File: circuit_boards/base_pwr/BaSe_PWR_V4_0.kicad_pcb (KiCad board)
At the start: 4 copper layers, 114.2 x 101.5 mm, 103 parts, among them J1 12VDC In, J10 Conn_01x04_Socket, J11 MOTOR, J12 USB3_A, J3 USB_B_Micro, J4 Conn_01x07_Pin, J5 Conn_02x06_Odd_Even, J6 USB3_B_Micro, J7 Conn_02x06_Odd_Even, J8 USB_C_Receptacle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

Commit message: almost finished layout
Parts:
- moved R4 3.05 mm to (82.8, 79.7), turned to 90 degrees
- moved D2 3.03 mm to (35.9, 85.0)
- moved R5 0.25 mm to (81.3, 83.0)
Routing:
- net /Taster_1: track 0.00 -> 34.6 mm, vias 0 -> 1
- net GND: track 18.7 -> 44.9 mm, vias 34 -> 56
- net /Taster_0: track 0.00 -> 24.2 mm, vias 0 -> 1
- net +3V3_STBY: track 12.2 -> 32.0 mm, vias 0 -> 9
- net /hmi_pwm0: track 0.00 -> 12.3 mm
- net /hmi_pwm1: track 0.00 -> 10.9 mm
- net /sw_sbu_on: track 37.1 -> 42.7 mm
- net /Dis_PWM: track 0.00 -> 4.32 mm
- net /LED_HMI: track 0.00 -> 4.26 mm
- net /sw_sbu_off: track 38.1 -> 41.4 mm
- net +5V: track 134.2 -> 136.5 mm
- net /vbus_sense: track 46.4 -> 45.7 mm
- net /~{LM2596S_ON}: track 47.0 -> 47.6 mm
- added copper zone on B.Cu, net +12V

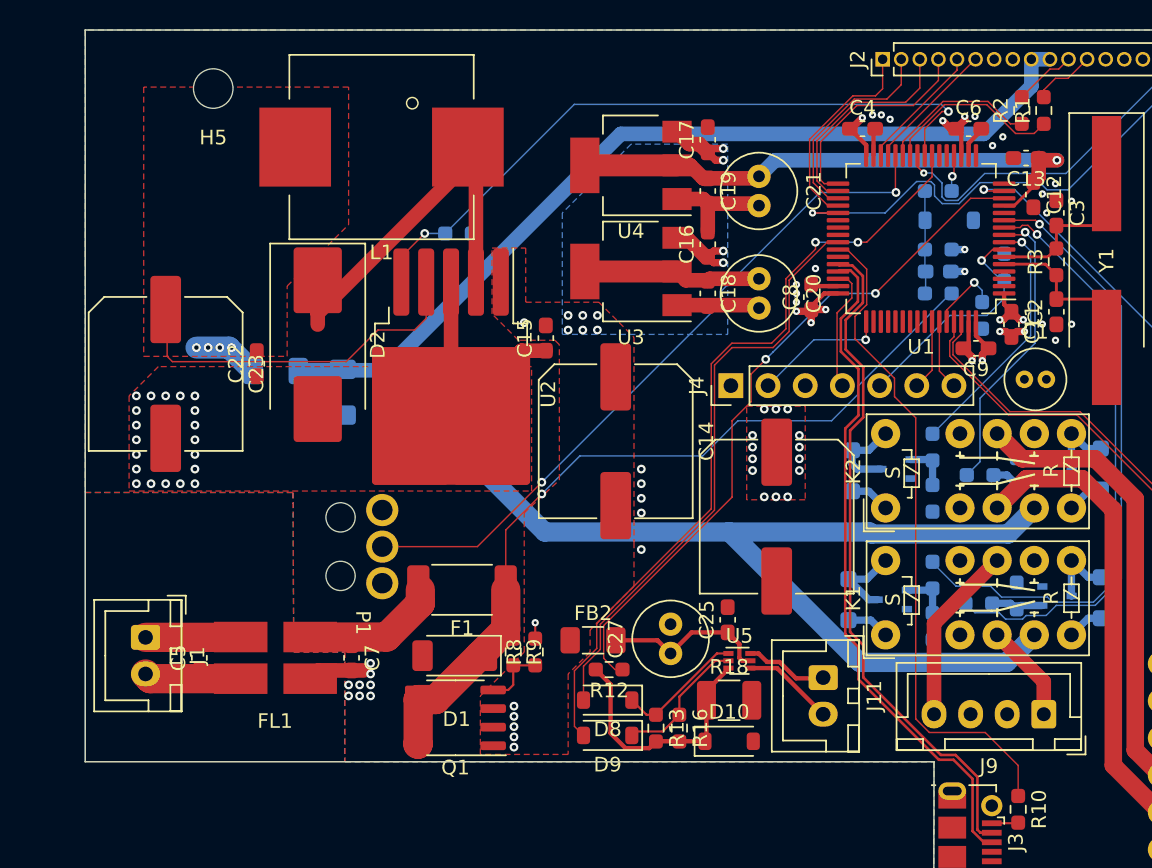
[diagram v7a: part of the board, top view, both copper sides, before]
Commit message: BaSe_PWR_V4_0: put DCDC coil to bottom, reduce loop area
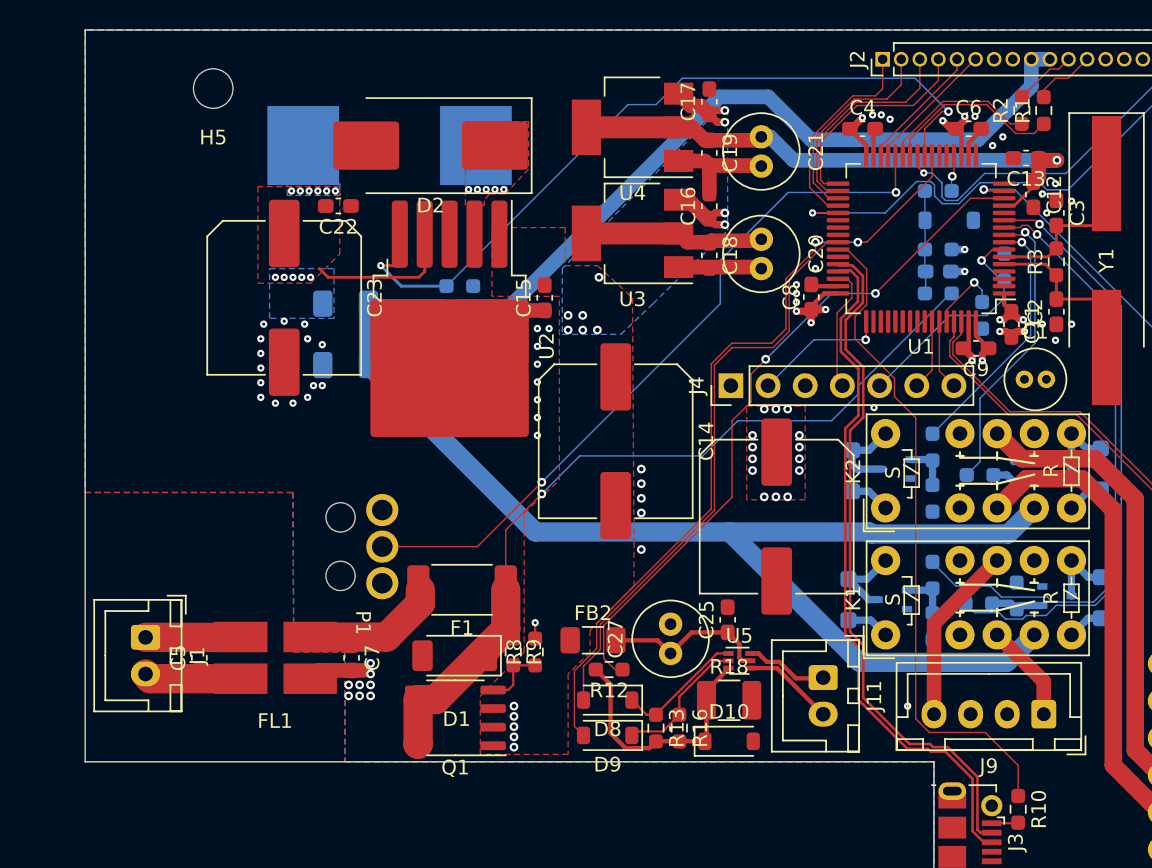
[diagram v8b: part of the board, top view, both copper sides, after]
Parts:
- L1: moved to B.Cu
- moved D2 15.6 mm to (43.6, 71.4), turned to 180 degrees
- moved C22 12.1 mm to (37.3, 75.5), turned to 180 degrees
- moved C23 9.63 mm to (33.6, 81.8)
- moved FB1 6.65 mm to (37.8, 82.2)
- moved R11 3.60 mm to (45.6, 81.0)
- moved U2 3.28 mm to (44.9, 85.1)
- moved C15 2.75 mm to (51.4, 81.8)
- moved C20 2.70 mm to (66.2, 77.8)
- moved C21 2.70 mm to (66.2, 70.8)
- moved C16 2.60 mm to (62.6, 75.5)
- moved C17 2.60 mm to (62.6, 68.4)
- moved C18 2.60 mm to (62.6, 78.9)
- moved C19 2.60 mm to (62.6, 71.9)
- moved U3 2.60 mm to (57.4, 77.4)
- moved U4 2.60 mm to (57.4, 70.2)
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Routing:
- net /SW: track 25.8 -> 0.00 mm, vias 0 -> 5
- net /+5v_out: track 29.3 -> 10.2 mm, vias 4 -> 11
- net /~{LM2596S_ON}: track 47.6 -> 53.6 mm
- net GND: track 44.9 -> 39.3 mm, vias 56 -> 61
- net +5V: track 136.5 -> 139.3 mm
- net /~{endswitch_undocked}: track 48.1 -> 49.4 mm
- net /USB_D-: track 46.5 -> 47.3 mm
- net /USB_D+: track 46.6 -> 47.4 mm
- net +12V: vias 30 -> 29
- added copper zone on B.Cu, net /+5v_out
- added copper zone on B.Cu, net /SW
- added copper zone on F.Cu, net /SW
